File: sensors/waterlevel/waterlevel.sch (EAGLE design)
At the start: 57 parts, among them IC1 LD117AS33TR, IC2 MCP604SL, IC3 MCP601SN, IC4 MCP601SN, P1 CAMDEN-CTB5000/6, U1 NCP1729SN35T1G, U2 SR05S05, U3 VISHAY-VCUT05A4, U4 VISHAY-VCUT05A4

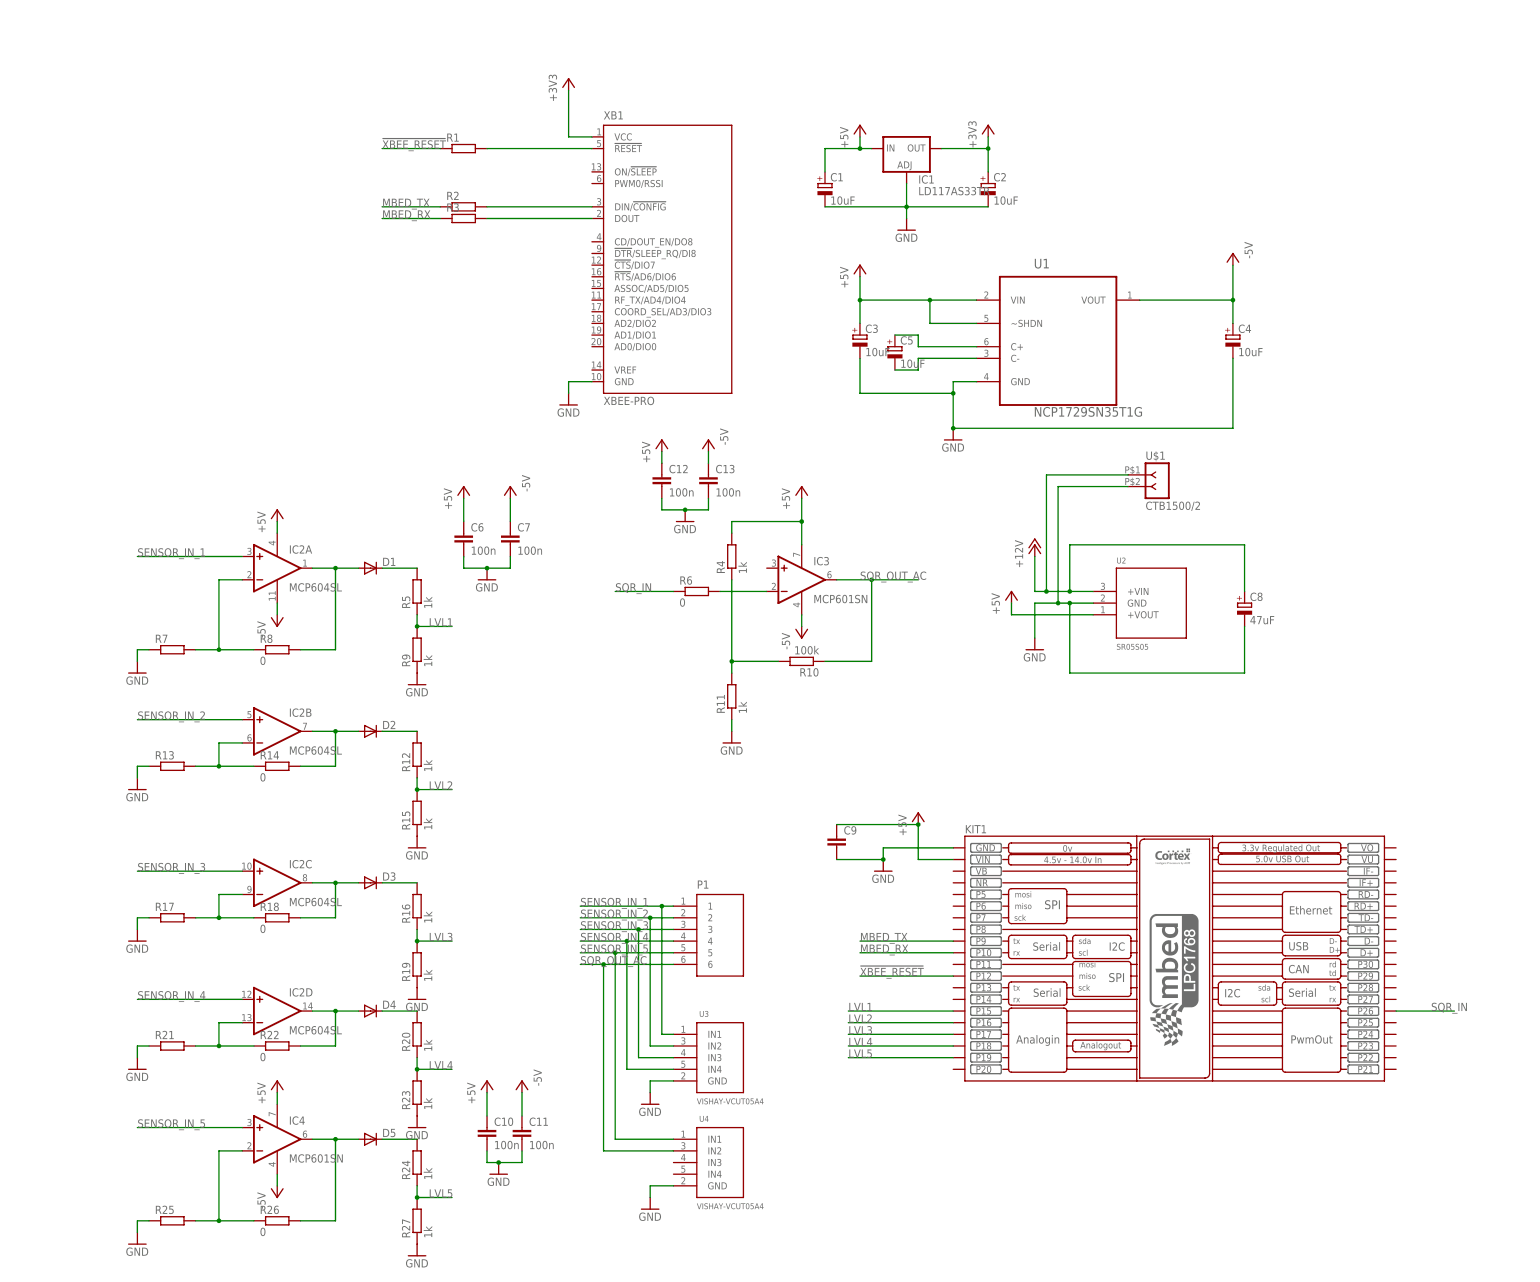
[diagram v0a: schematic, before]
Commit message: Completed layout of water level sensor.
TODO:
Check circuit
Add status LEDs
Add bias resistors to GND
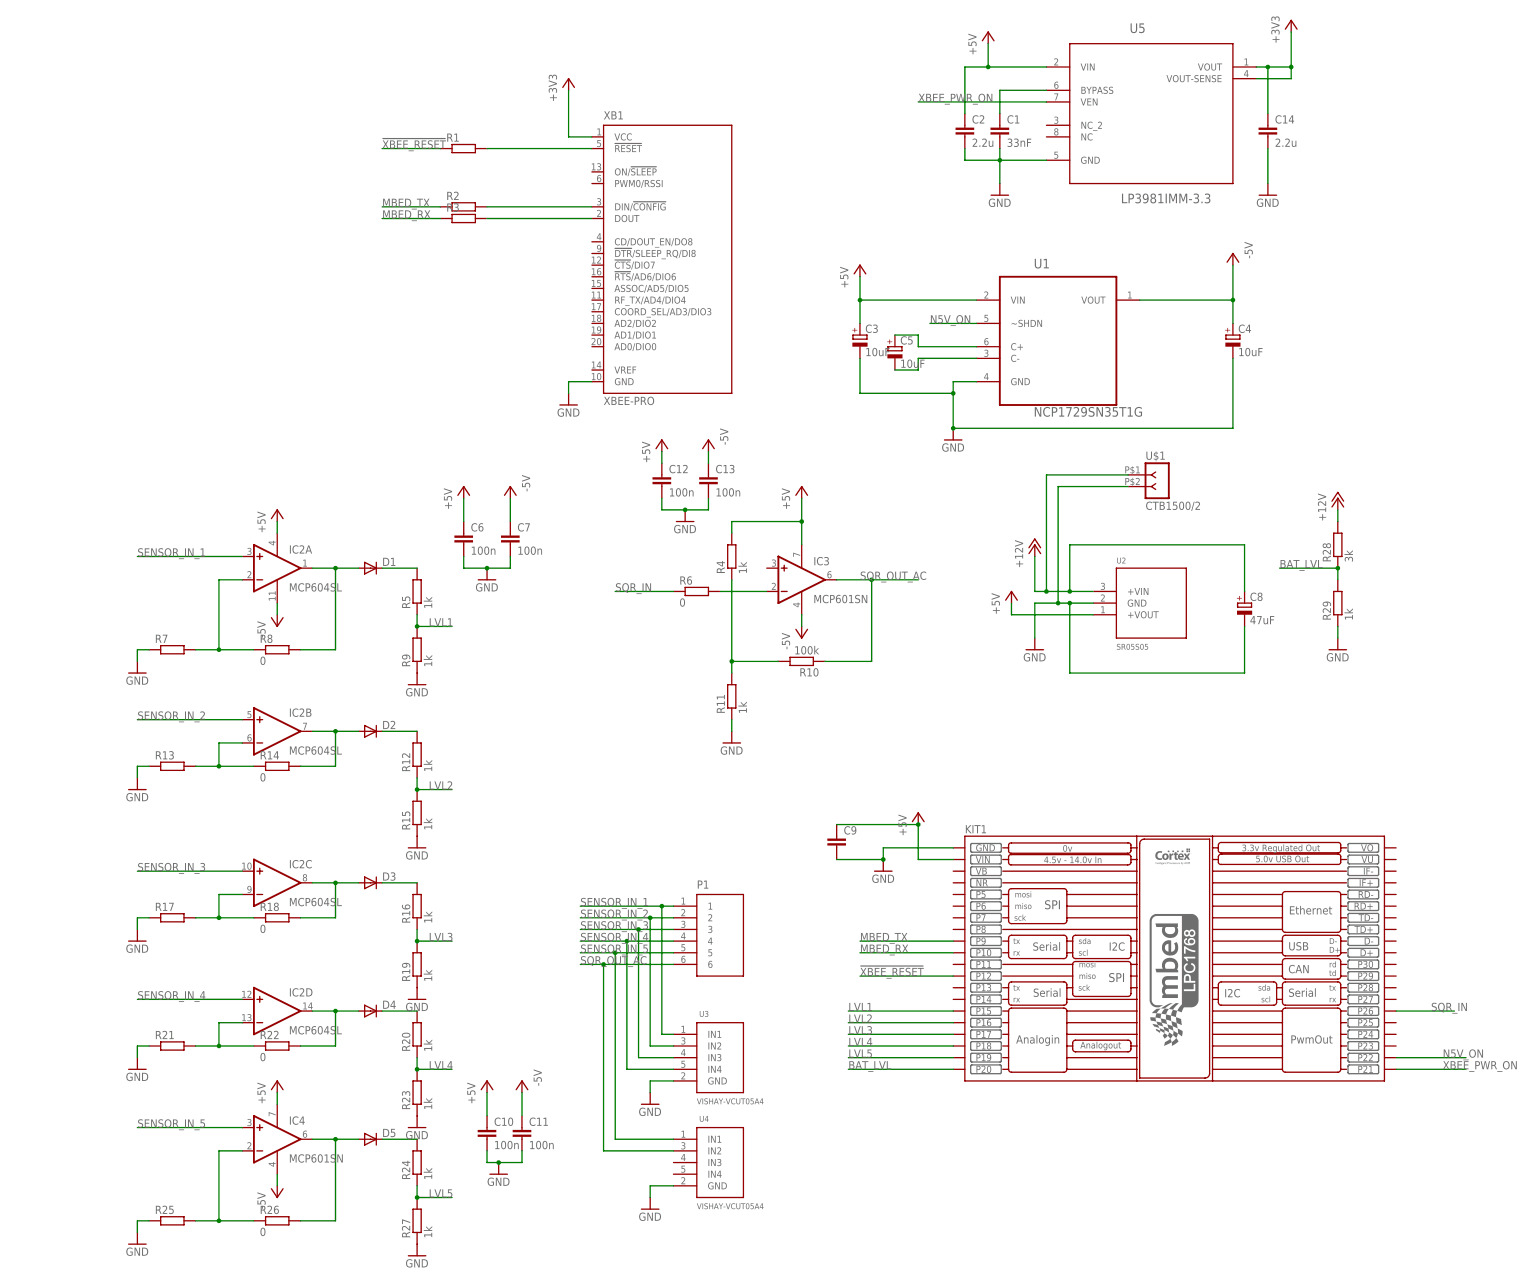
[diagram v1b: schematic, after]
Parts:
- removed IC1: LD117AS33TR, v-reg:LD117AS33TR
- added C14: 2.2u, resistor:C-EUC0603
- added R28: 3k, resistor:R-EU_R0805
- added R29: 1k, resistor:R-EU_R0805
- added U5: LP3981IMM-3.3, eko-parts:LP3981IMM-3.3
- C1: value 10uF -> 33nF; device resistor:CPOL-EUB/3528-21R -> resistor:C-EUC0603
- C2: value 10uF -> 2.2u; device resistor:CPOL-EUB/3528-21R -> resistor:C-EUC0603; FARNELL (none) -> 1759400
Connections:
- new net BAT_LVL: KIT1.P20, R28.1, R29.2
- new net N$28: C1.1, U5.BYPASS
- new net N5V_ON: KIT1.P22, U1.~SHDN
- new net XBEE_PWR_ON: KIT1.P21, U5.VEN
- net +12V: now also R28.2
- net +3V3: now also C14.1, U5.VOUT, U5.VOUT-SENSE; no longer C2.+, IC1.OUT
- net +5V: now also C2.1, U5.VIN; no longer C1.+, IC1.IN, U1.~SHDN
- net GND: now also C1.2, C14.2, C2.2, R29.1, U5.GND; no longer C1.-, C2.-, IC1.ADJ

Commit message: Added LEDs and Bias Resistors to water sensor
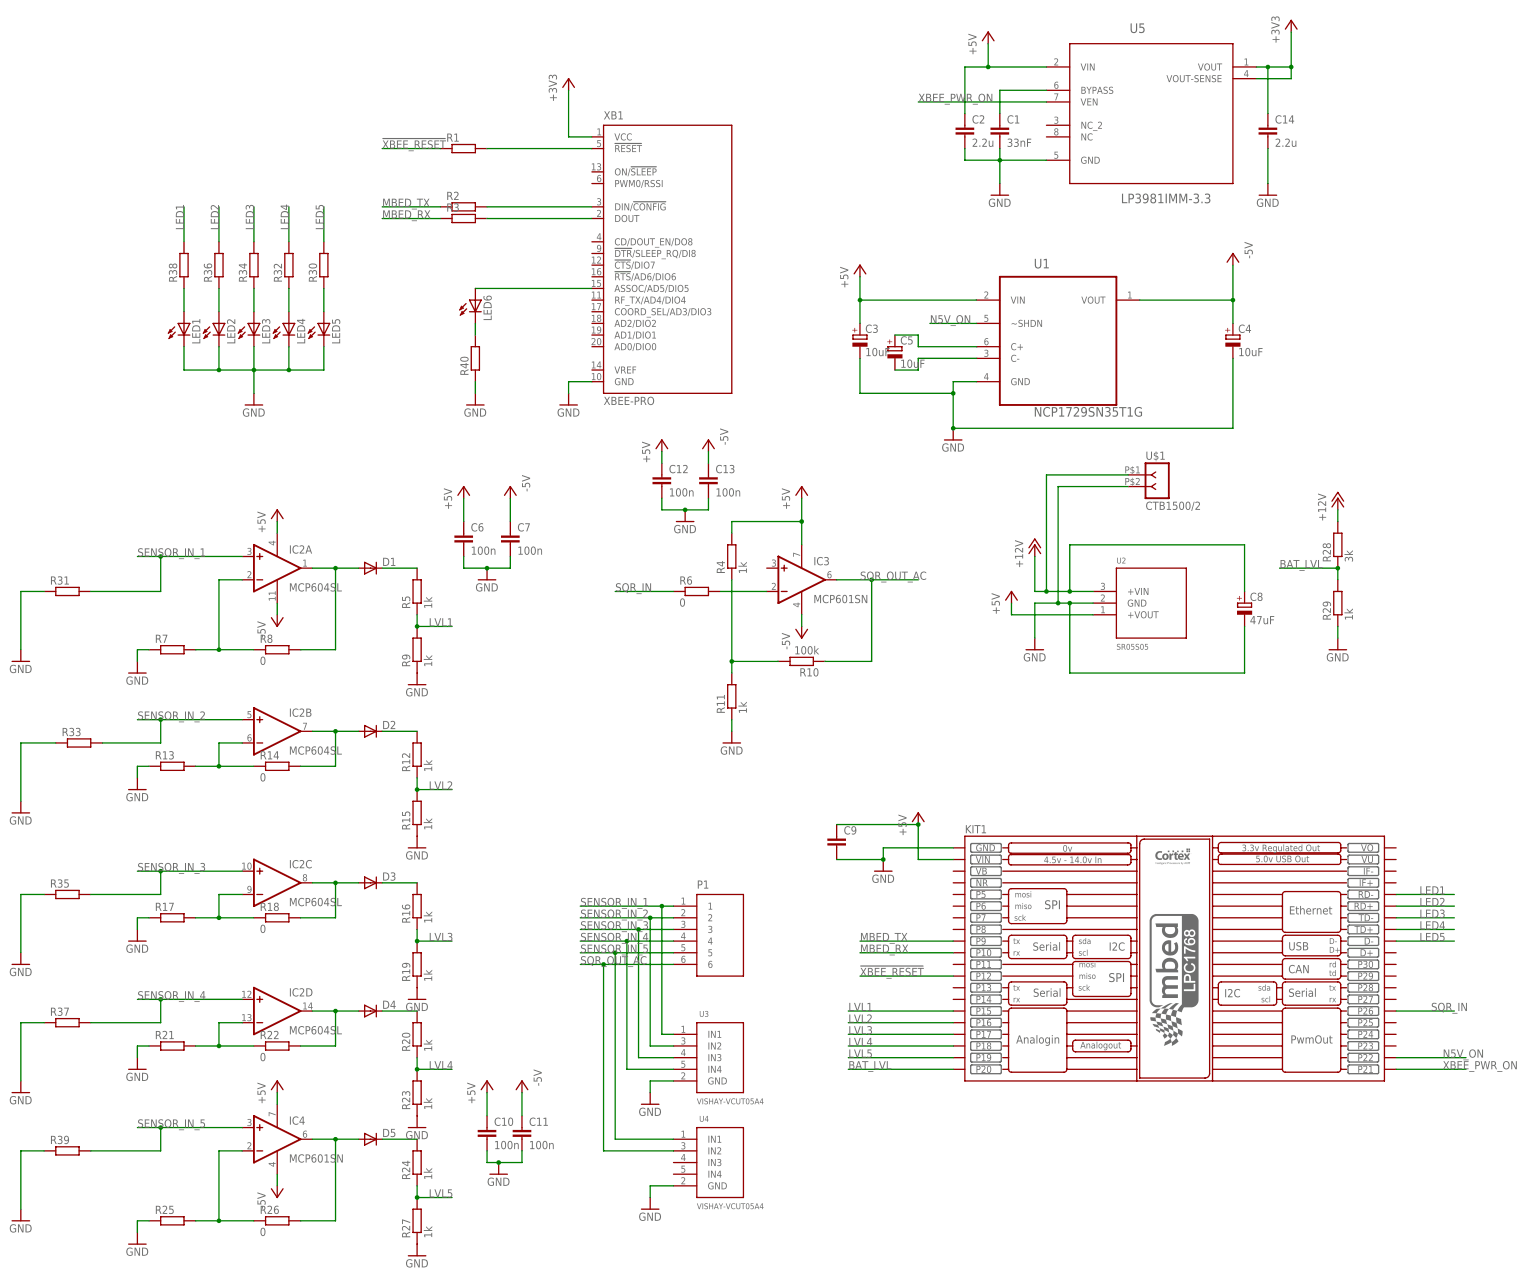
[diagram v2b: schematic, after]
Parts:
- added LED1, LED2, LED3, LED4, LED5, LED6: (no value), led:LEDCHIPLED_0805
- added R30, R32, R34, R36, R38, R40: (no value), resistor:R-EU_R0603
- added R31, R33, R35, R37, R39: (no value), resistor:R-EU_R0805
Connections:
- new net LED1: KIT1.RD-, R38.2
- new net LED2: KIT1.RD+, R36.2
- new net LED3: KIT1.TD-, R34.2
- new net LED4: KIT1.TD+, R32.2
- new net LED5: KIT1.D-, R30.2
- new net N$17: LED6.A, XB1.ASSOC/AD5/DIO5
- new net N$24: LED6.C, R40.2
- new net N$25: LED5.A, R30.1
- new net N$26: LED4.A, R32.1
- new net N$27: LED3.A, R34.1
- new net N$29: LED2.A, R36.1
- new net N$30: LED1.A, R38.1
- net GND: now also LED1.C, LED2.C, LED3.C, LED4.C, LED5.C, R31.1, R33.1, R35.1, R37.1, R39.1, R40.1
- net SENSOR_IN_1: now also R31.2
- net SENSOR_IN_2: now also R33.2
- net SENSOR_IN_3: now also R35.2
- net SENSOR_IN_4: now also R37.2
- net SENSOR_IN_5: now also R39.2
